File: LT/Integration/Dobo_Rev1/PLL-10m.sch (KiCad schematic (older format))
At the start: 49 parts, among them Q3 Q_NJFET_DSG, Q4 Q_NJFET_DSG, U3 L7808, U4 LMX231X

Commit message: Daughter Board
Began annotating the rest of the Daughter board
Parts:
- L2: footprint (none) -> Inductor_SMD:L_0805_2012Metric
- R14, R15, R16, R17, R18, R19, R20, R21, R22, R23, R24, R25, R26: footprint (none) -> Resistor_SMD:R_0805_2012Metric
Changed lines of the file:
@@
 F 0 "R26" H 7270 2896 50  0000 L CNN
 F 1 "18" H 7270 2805 50  0000 L CNN
-F 2 "" V 7130 2850 50  0001 C CNN
+F 2 "Resistor_SMD:R_0805_2012Metric" V 7130 2850 50  0001 C CNN
 F 3 "~" H 7200 2850 50  0001 C CNN
 	1    7200 2850
@@
 F 0 "R17" H 6320 2746 50  0000 L CNN
 F 1 "18" H 6320 2655 50  0000 L CNN
-F 2 "" V 6180 2700 50  0001 C CNN
+F 2 "Resistor_SMD:R_0805_2012Metric" V 6180 2700 50  0001 C CNN
 F 3 "~" H 6250 2700 50  0001 C CNN
 	1    6250 2700
@@
 F 0 "R22" H 6820 2746 50  0000 L CNN
 F 1 "18" H 6820 2655 50  0000 L CNN
-F 2 "" V 6680 2700 50  0001 C CNN
+F 2 "Resistor_SMD:R_0805_2012Metric" V 6680 2700 50  0001 C CNN
 F 3 "~" H 6750 2700 50  0001 C CNN
 	1    6750 2700
@@
 F 0 "R14" H 6070 1846 50  0000 L CNN
 F 1 "10k" H 6070 1755 50  0000 L CNN
-F 2 "" V 5930 1800 50  0001 C CNN
+F 2 "Resistor_SMD:R_0805_2012Metric" V 5930 1800 50  0001 C CNN
 F 3 "~" H 6000 1800 50  0001 C CNN
 	1    6000 1800
@@
 F 0 "L2" V 8954 3778 50  0000 L CNN
 F 1 "1.8uH" V 9045 3778 50  0000 L CNN
-F 2 "" H 9000 3700 50  0001 C CNN
+F 2 "Inductor_SMD:L_0805_2012Metric" H 9000 3700 50  0001 C CNN
 F 3 "~" H 9000 3700 50  0001 C CNN
 	1    9000 3700
@@
 F 0 "R15" H 6070 2346 50  0000 L CNN
 F 1 "3.3k" H 6070 2255 50  0000 L CNN
-F 2 "" V 5930 2300 50  0001 C CNN
+F 2 "Resistor_SMD:R_0805_2012Metric" V 5930 2300 50  0001 C CNN
 F 3 "~" H 6000 2300 50  0001 C CNN
 	1    6000 2300
@@
 F 0 "R25" H 7100 2300 50  0000 L CNN
 F 1 "100k" H 7100 2200 50  0000 L CNN
-F 2 "" V 6980 2350 50  0001 C CNN
+F 2 "Resistor_SMD:R_0805_2012Metric" V 6980 2350 50  0001 C CNN
 F 3 "~" H 7050 2350 50  0001 C CNN
 	1    7050 2350
@@
 F 0 "R18" H 6420 2296 50  0000 L CNN
 F 1 "3.3k" H 6420 2205 50  0000 L CNN
-F 2 "" V 6280 2250 50  0001 C CNN
+F 2 "Resistor_SMD:R_0805_2012Metric" V 6280 2250 50  0001 C CNN
 F 3 "~" H 6350 2250 50  0001 C CNN
 	1    6350 2250
@@
 F 0 "R20" V 6850 1800 50  0000 C CNN
 F 1 "R" V 6750 1750 50  0000 C CNN
-F 2 "" V 6580 1750 50  0001 C CNN
+F 2 "Resistor_SMD:R_0805_2012Metric" V 6580 1750 50  0001 C CNN
 F 3 "~" H 6650 1750 50  0001 C CNN
 	1    6650 1750
@@
 F 0 "R19" H 6300 1700 50  0000 C CNN
 F 1 "R" H 6300 1800 50  0000 C CNN
-F 2 "" V 6330 1750 50  0001 C CNN
+F 2 "Resistor_SMD:R_0805_2012Metric" V 6330 1750 50  0001 C CNN
 F 3 "~" H 6400 1750 50  0001 C CNN
 	1    6400 1750
@@
 F 0 "R21" V 6500 2350 50  0000 L CNN
 F 1 "0 Ohms" V 6600 2200 50  0000 L CNN
-F 2 "" V 6630 2300 50  0001 C CNN
+F 2 "Resistor_SMD:R_0805_2012Metric" V 6630 2300 50  0001 C CNN
 F 3 "~" H 6700 2300 50  0001 C CNN
 	1    6700 2300
@@
 F 0 "R23" V 7000 3100 50  0000 C CNN
 F 1 "R" V 6900 3050 50  0000 C CNN
-F 2 "" V 6730 3050 50  0001 C CNN
+F 2 "Resistor_SMD:R_0805_2012Metric" V 6730 3050 50  0001 C CNN
 F 3 "~" H 6800 3050 50  0001 C CNN
 	1    6800 3050
@@
 F 0 "R16" V 6200 2650 50  0000 L CNN
 F 1 "1k" V 6100 2650 50  0000 L CNN
-F 2 "" V 5930 2700 50  0001 C CNN
+F 2 "Resistor_SMD:R_0805_2012Metric" V 5930 2700 50  0001 C CNN
 F 3 "~" H 6000 2700 50  0001 C CNN
 	1    6000 2700
@@
 F 0 "R24" V 6850 2000 50  0000 C CNN
 F 1 "10k" V 6834 1750 50  0000 C CNN
-F 2 "" V 6880 1750 50  0001 C CNN
+F 2 "Resistor_SMD:R_0805_2012Metric" V 6880 1750 50  0001 C CNN
 F 3 "~" H 6950 1750 50  0001 C CNN
 	1    6950 1750

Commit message: Finished Daughter Board
I finished assigning the footprints to the daughter board
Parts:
- Q3, Q4: footprint (none) -> Package_TO_SOT_THT:TO-251-3_Vertical
- U3: footprint (none) -> Package_TO_SOT_THT:TO-220-3_Vertical
- U4: footprint (none) -> LT:LMX231X
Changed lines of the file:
@@
 F 0 "U3" H 4050 1750 50  0000 C CNN
 F 1 "L7808" H 4050 1841 50  0000 C CNN
-F 2 "" H 4075 1450 50  0001 L CIN
+F 2 "Package_TO_SOT_THT:TO-220-3_Vertical" H 4075 1450 50  0001 L CIN
 F 3 "http://www.st.com/content/ccc/resource/technical/document/datasheet/41/4f/b3/b0/12/d4/47/88/CD00000444.pdf/files/CD00000444.pdf/jcr:content/translations/en.CD00000444.pdf" H 4050 1550 50  0001 C CNN
 	1    4050 1600
@@
 F 0 "U4" H 3950 1250 50  0000 C CNN
 F 1 "LMX231X" H 3950 1150 50  0000 C CNN
-F 2 "" H 3600 1700 50  0001 C CNN
+F 2 "LT:LMX231X" H 3600 1700 50  0001 C CNN
 F 3 "" H 3600 1700 50  0001 C CNN
 	1    4100 2000
@@
 F 0 "Q4" H 7591 4246 50  0000 L CNN
 F 1 "Q_NJFET_DSG" H 7591 4155 50  0000 L CNN
-F 2 "" H 7600 4300 50  0001 C CNN
+F 2 "Package_TO_SOT_THT:TO-251-3_Vertical" H 7600 4300 50  0001 C CNN
 F 3 "~" H 7400 4200 50  0001 C CNN
 	1    7400 4200
@@
 F 0 "Q3" H 7291 3796 50  0000 L CNN
 F 1 "Q_NJFET_DSG" H 7291 3705 50  0000 L CNN
-F 2 "" H 7300 3850 50  0001 C CNN
+F 2 "Package_TO_SOT_THT:TO-251-3_Vertical" H 7300 3850 50  0001 C CNN
 F 3 "~" H 7100 3750 50  0001 C CNN
 	1    7100 3750

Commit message: Messing With Resistors
Just doing some resistor changes but idk if it worked
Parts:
- R14, R15, R16, R17, R18, R19, R20, R21, R22, R23, R24, R25, R26: symbol Device:R -> Dobo_Rev1-rescue:R-Device
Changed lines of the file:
@@
 $EndComp
 $Comp
-L Device:R R?
+L Dobo_Rev1-rescue:R-Device R?
 U 1 1 5E4E1517
 P 7200 2850
@@
 $EndComp
 $Comp
-L Device:R R?
+L Dobo_Rev1-rescue:R-Device R?
 U 1 1 5E4E151D
 P 6250 2700
@@
 $EndComp
 $Comp
-L Device:R R?
+L Dobo_Rev1-rescue:R-Device R?
 U 1 1 5E4E1523
 P 6750 2700
@@
 $EndComp
 $Comp
-L Device:R R?
+L Dobo_Rev1-rescue:R-Device R?
 U 1 1 5E4E1529
 P 6000 1800
@@
 $EndComp
 $Comp
-L Device:R R?
+L Dobo_Rev1-rescue:R-Device R?
 U 1 1 5E4E1595
 P 6000 2300
@@
 $EndComp
 $Comp
-L Device:R R?
+L Dobo_Rev1-rescue:R-Device R?
 U 1 1 5E4E159B
 P 7050 2350
@@
 $EndComp
 $Comp
-L Device:R R?
+L Dobo_Rev1-rescue:R-Device R?
 U 1 1 5E4E15A1
 P 6350 2250
@@
 $EndComp
 $Comp
-L Device:R R?
+L Dobo_Rev1-rescue:R-Device R?
 U 1 1 5E4E15C6
 P 6650 1750
@@
 $EndComp
 $Comp
-L Device:R R?
+L Dobo_Rev1-rescue:R-Device R?
 U 1 1 5E4E15D8
 P 6400 1750
@@
 $EndComp
 $Comp
-L Device:R R?
+L Dobo_Rev1-rescue:R-Device R?
 U 1 1 5E4E15F0
 P 6700 2300
@@
 $EndComp
 $Comp
-L Device:R R?
+L Dobo_Rev1-rescue:R-Device R?
 U 1 1 5E4E15FC
 P 6800 3050
@@
 $EndComp
 $Comp
-L Device:R R?
+L Dobo_Rev1-rescue:R-Device R?
 U 1 1 5E4E1608
 P 6000 2700
@@
 $EndComp
 $Comp
-L Device:R R?
+L Dobo_Rev1-rescue:R-Device R?
 U 1 1 5E4E162C
 P 6950 1750

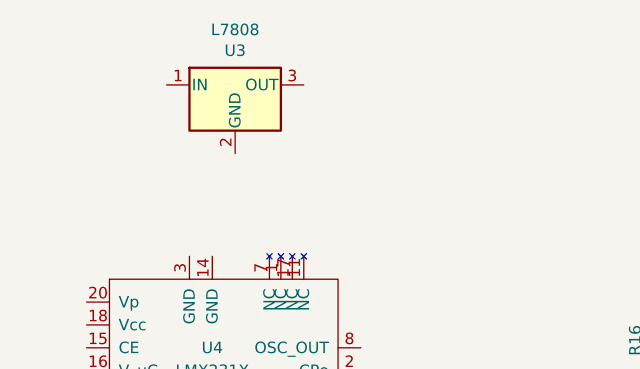
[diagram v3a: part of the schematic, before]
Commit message: finshed assigning step files for integration boards
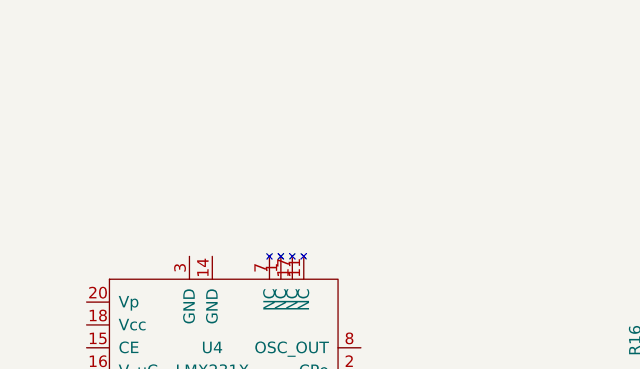
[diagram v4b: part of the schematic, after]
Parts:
- removed U3: L7808, Package_TO_SOT_THT:TO-220-3_Vertical, symbol Regulator_Linear:L7808
- Q3, Q4: footprint Package_TO_SOT_THT:TO-251-3_Vertical -> Package_TO_SOT_THT:TO-92_Inline_Wide
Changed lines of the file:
@@
 EESchema Schematic File Version 4
-LIBS:Dobo_Rev1-cache
-EELAYER 26 0
+EELAYER 30 0
 EELAYER END
 $Descr A4 11693 8268
@@
 $EndComp
 $Comp
-L Regulator_Linear:L7808 U?
-U 1 1 5E4E1565
-P 4050 1600
-AR Path="/5E4B185A/5E4E1565" Ref="U?"  Part="1"
-AR Path="/5E4DD63E/5E4E1565" Ref="U3"  Part="1"
-F 0 "U3" H 4050 1750 50  0000 C CNN
-F 1 "L7808" H 4050 1841 50  0000 C CNN
-F 2 "Package_TO_SOT_THT:TO-220-3_Vertical" H 4075 1450 50  0001 L CIN
-F 3 "http://www.st.com/content/ccc/resource/technical/document/datasheet/41/4f/b3/b0/12/d4/47/88/CD00000444.pdf/files/CD00000444.pdf/jcr:content/translations/en.CD00000444.pdf" H 4050 1550 50  0001 C CNN
-	1    4050 1600
-	1    0    0    -1
-$EndComp
-$Comp
 L Device:C C?
 U 1 1 5E4E156B
@@
 F 0 "Q4" H 7591 4246 50  0000 L CNN
 F 1 "Q_NJFET_DSG" H 7591 4155 50  0000 L CNN
-F 2 "Package_TO_SOT_THT:TO-251-3_Vertical" H 7600 4300 50  0001 C CNN
+F 2 "Package_TO_SOT_THT:TO-92_Inline_Wide" H 7600 4300 50  0001 C CNN
 F 3 "~" H 7400 4200 50  0001 C CNN
 	1    7400 4200
@@
 F 0 "Q3" H 7291 3796 50  0000 L CNN
 F 1 "Q_NJFET_DSG" H 7291 3705 50  0000 L CNN
-F 2 "Package_TO_SOT_THT:TO-251-3_Vertical" H 7300 3850 50  0001 C CNN
+F 2 "Package_TO_SOT_THT:TO-92_Inline_Wide" H 7300 3850 50  0001 C CNN
 F 3 "~" H 7100 3750 50  0001 C CNN
 	1    7100 3750
